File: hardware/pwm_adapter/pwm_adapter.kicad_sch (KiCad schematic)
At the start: 59 parts, among them J1 WAGO250-204, J10 Conn_01x06_Female, J11 Conn_01x06_Female, J12 Conn_01x06_Female, J13 Conn_01x06_Female, J14 Conn_01x03, J15 Conn_01x06_Female, J16 Conn_01x06_Female, J17 Conn_01x06_Female, J18 Conn_01x06_Female, J19 Button-Sensors-MicroMatch2X03, J2 WAGO250-208, J20 Conn_01x06_Female, J21 Conn_01x06_Female, J22 Conn_01x06_Female, J23 Conn_01x06_Female, J24 Conn_01x06_Female, J25 Conn_01x06_Female, J26 Conn_01x06_Female, J27 Conn_01x06_Female, J3 WAGO250-208, J4 WAGO250-208, J5 WAGO250-208, J6 WAGO250-208, J7 WAGO250-208, J8 WAGO250-208, J9 WAGO250-208, U1 DHT11, U2 PCA9685PW, U3 PCA9685PW

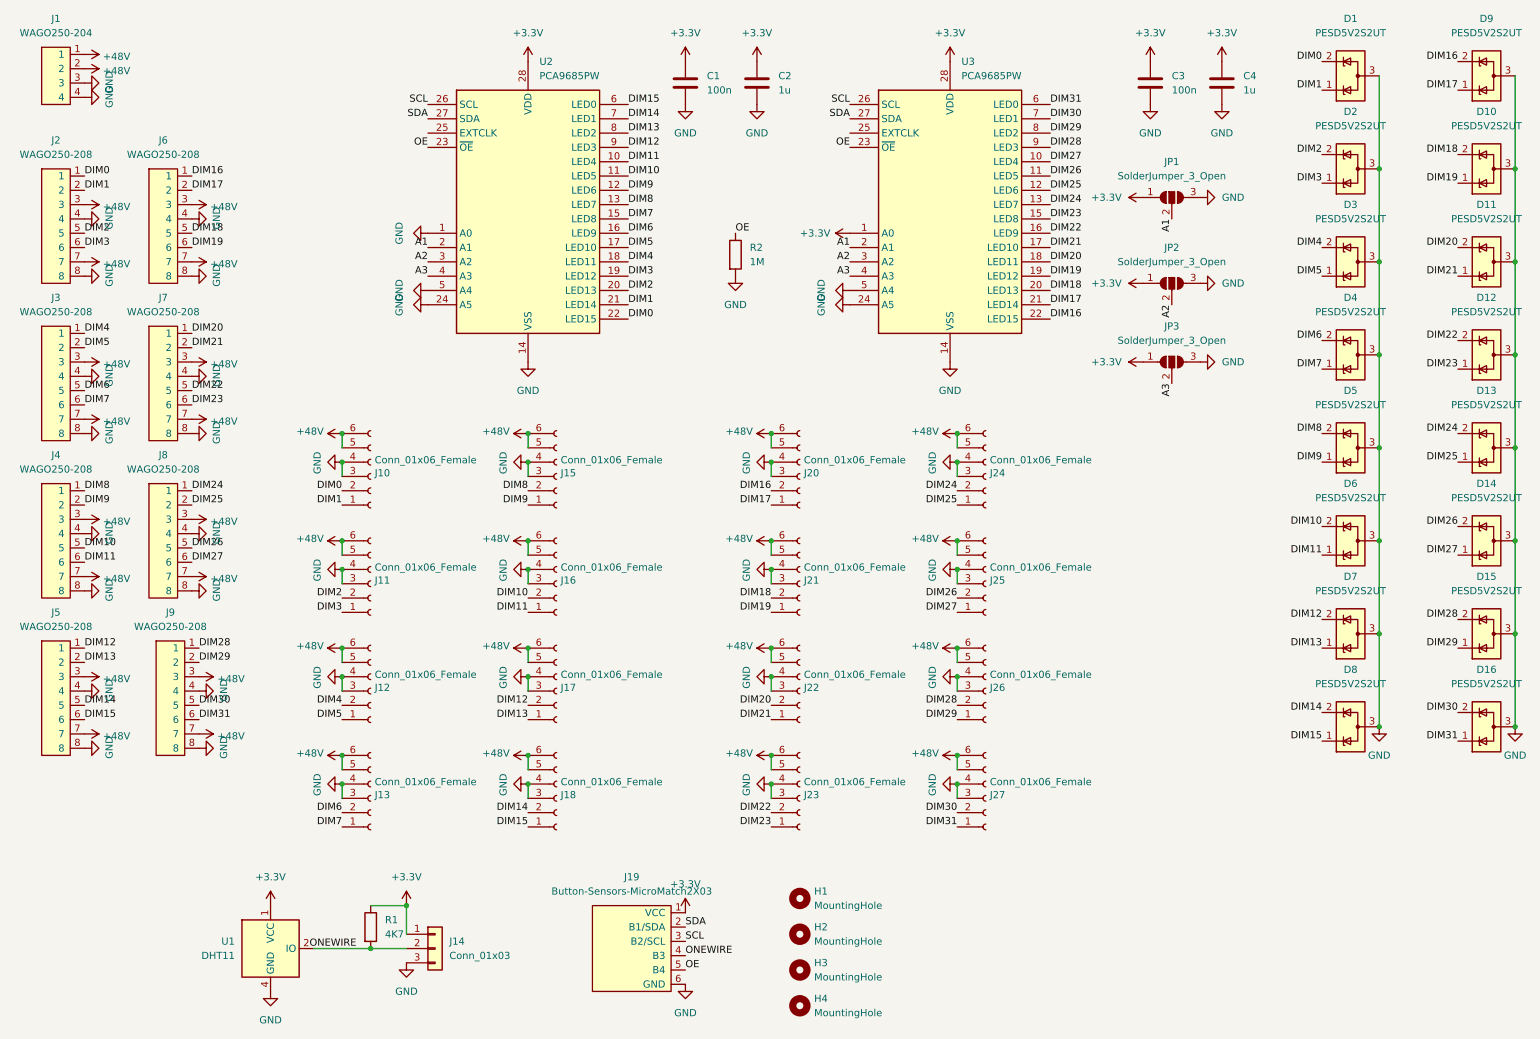
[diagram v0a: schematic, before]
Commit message: feat: Add fab export options for all pcbs
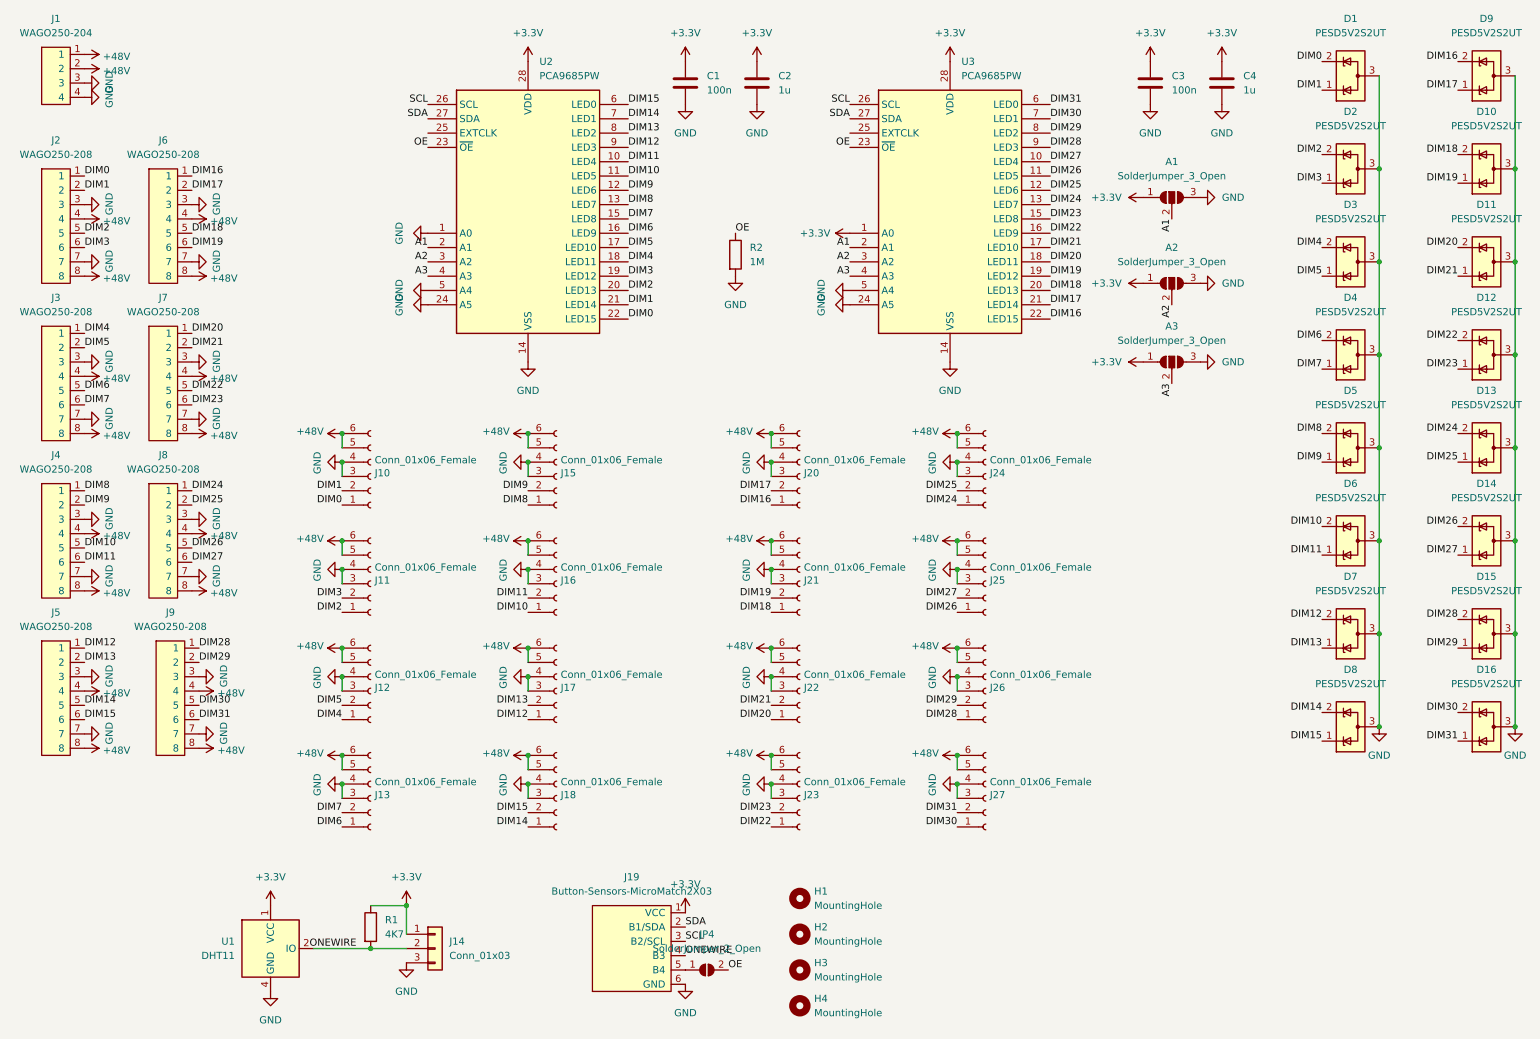
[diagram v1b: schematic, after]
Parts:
- added JP4: SolderJumper_2_Open, Jumper:SolderJumper-2_P1.3mm_Open_RoundedPad1.0x1.5mm, symbol Jumper:SolderJumper_2_Open
- H1, H2, H3, H4: footprint MountingHole:MountingHole_3.2mm_M3_DIN965 -> MountingHole:MountingHole_4.3mm_M4_DIN965
- renumbered JP1 to A1, JP2 to A2, JP3 to A3
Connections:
- net +48V: now also J2.4, J2.8, J3.4, J3.8, J4.4, J4.8, J5.4, J5.8, J6.4, J6.8, J7.4, J7.8, J8.4, J8.8, J9.4, J9.8; no longer J2.3, J2.7, J3.3, J3.7, J4.3, J4.7, J5.3, J5.7, J6.3, J6.7, J7.3, J7.7, J8.3, J8.7, J9.3, J9.7
- net DIM0: now also J10.1 (Pin_1); no longer J10.2 (Pin_2)
- net DIM1: now also J10.2 (Pin_2); no longer J10.1 (Pin_1)
- net DIM10: now also J16.1 (Pin_1); no longer J16.2 (Pin_2)
- net DIM11: now also J16.2 (Pin_2); no longer J16.1 (Pin_1)
- net DIM12: now also J17.1 (Pin_1); no longer J17.2 (Pin_2)
- net DIM13: now also J17.2 (Pin_2); no longer J17.1 (Pin_1)
- net DIM14: now also J18.1 (Pin_1); no longer J18.2 (Pin_2)
- net DIM15: now also J18.2 (Pin_2); no longer J18.1 (Pin_1)
- net DIM16: now also J20.1 (Pin_1); no longer J20.2 (Pin_2)
- net DIM17: now also J20.2 (Pin_2); no longer J20.1 (Pin_1)
- net DIM18: now also J21.1 (Pin_1); no longer J21.2 (Pin_2)
- net DIM19: now also J21.2 (Pin_2); no longer J21.1 (Pin_1)
- net DIM2: now also J11.1 (Pin_1); no longer J11.2 (Pin_2)
- net DIM20: now also J22.1 (Pin_1); no longer J22.2 (Pin_2)
- net DIM21: now also J22.2 (Pin_2); no longer J22.1 (Pin_1)
- net DIM22: now also J23.1 (Pin_1); no longer J23.2 (Pin_2)
- net DIM23: now also J23.2 (Pin_2); no longer J23.1 (Pin_1)
- net DIM24: now also J24.1 (Pin_1); no longer J24.2 (Pin_2)
- net DIM25: now also J24.2 (Pin_2); no longer J24.1 (Pin_1)
- net DIM26: now also J25.1 (Pin_1); no longer J25.2 (Pin_2)
- net DIM27: now also J25.2 (Pin_2); no longer J25.1 (Pin_1)
- net DIM28: now also J26.1 (Pin_1); no longer J26.2 (Pin_2)
- net DIM29: now also J26.2 (Pin_2); no longer J26.1 (Pin_1)
- net DIM3: now also J11.2 (Pin_2); no longer J11.1 (Pin_1)
- net DIM30: now also J27.1 (Pin_1); no longer J27.2 (Pin_2)
- net DIM31: now also J27.2 (Pin_2); no longer J27.1 (Pin_1)
- net DIM4: now also J12.1 (Pin_1); no longer J12.2 (Pin_2)
- net DIM5: now also J12.2 (Pin_2); no longer J12.1 (Pin_1)
- net DIM6: now also J13.1 (Pin_1); no longer J13.2 (Pin_2)
- net DIM7: now also J13.2 (Pin_2); no longer J13.1 (Pin_1)
- net DIM8: now also J15.1 (Pin_1); no longer J15.2 (Pin_2)
- net DIM9: now also J15.2 (Pin_2); no longer J15.1 (Pin_1)
- net GND: now also J2.3, J2.7, J3.3, J3.7, J4.3, J4.7, J5.3, J5.7, J6.3, J6.7, J7.3, J7.7, J8.3, J8.7, J9.3, J9.7; no longer J2.4, J2.8, J3.4, J3.8, J4.4, J4.8, J5.4, J5.8, J6.4, J6.8, J7.4, J7.8, J8.4, J8.8, J9.4, J9.8
- net OE: now also JP4.2 (B); no longer J19.5 (B4)
- new net: J19.5 (B4), JP4.1 (A)

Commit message: fix: Add GND to ext_clk_in
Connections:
- net GND: now also U2.25 (EXTCLK), U3.25 (EXTCLK)
